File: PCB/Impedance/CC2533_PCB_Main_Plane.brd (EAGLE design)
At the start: 69.5 x 40.3 mm, 34 parts

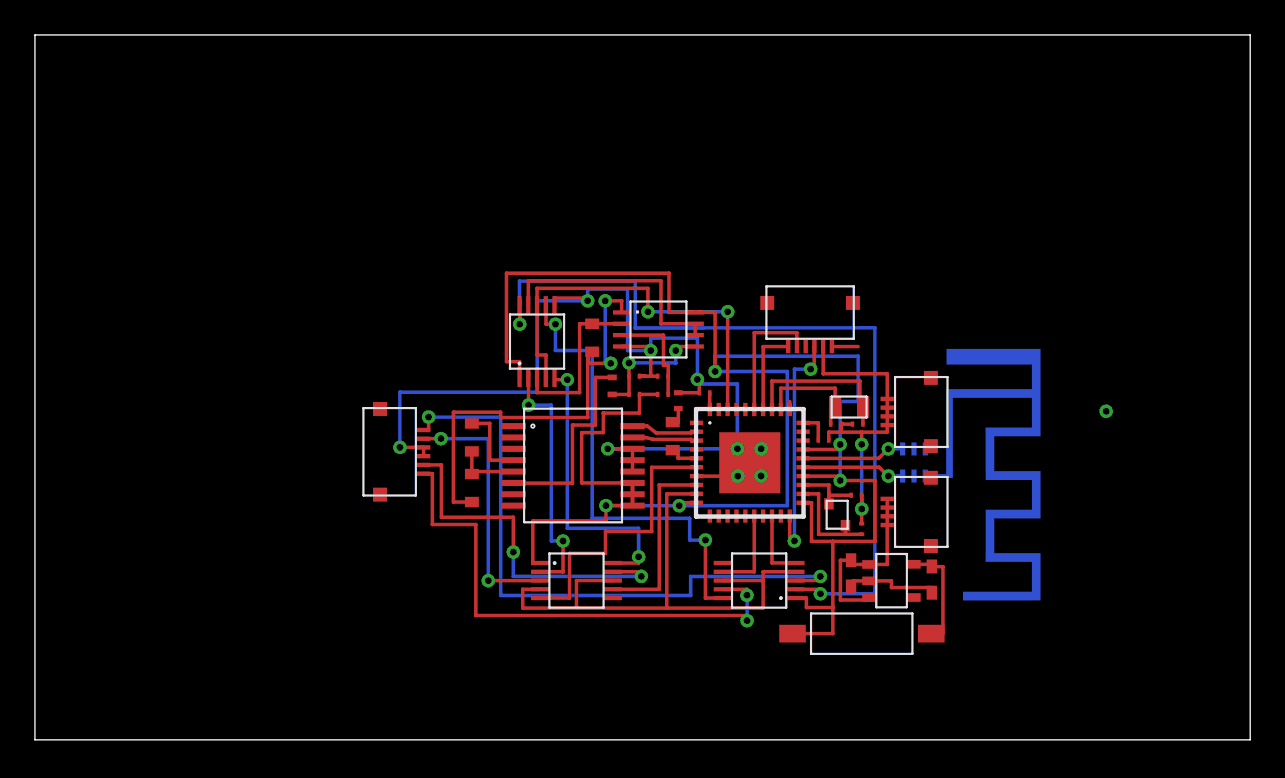
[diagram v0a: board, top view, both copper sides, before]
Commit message: New updates
Added new layout of CC2533 voltage stim and AD5933 impeance analysis
with ground planes (completed), and that of AD5933 impedance analysis
only.
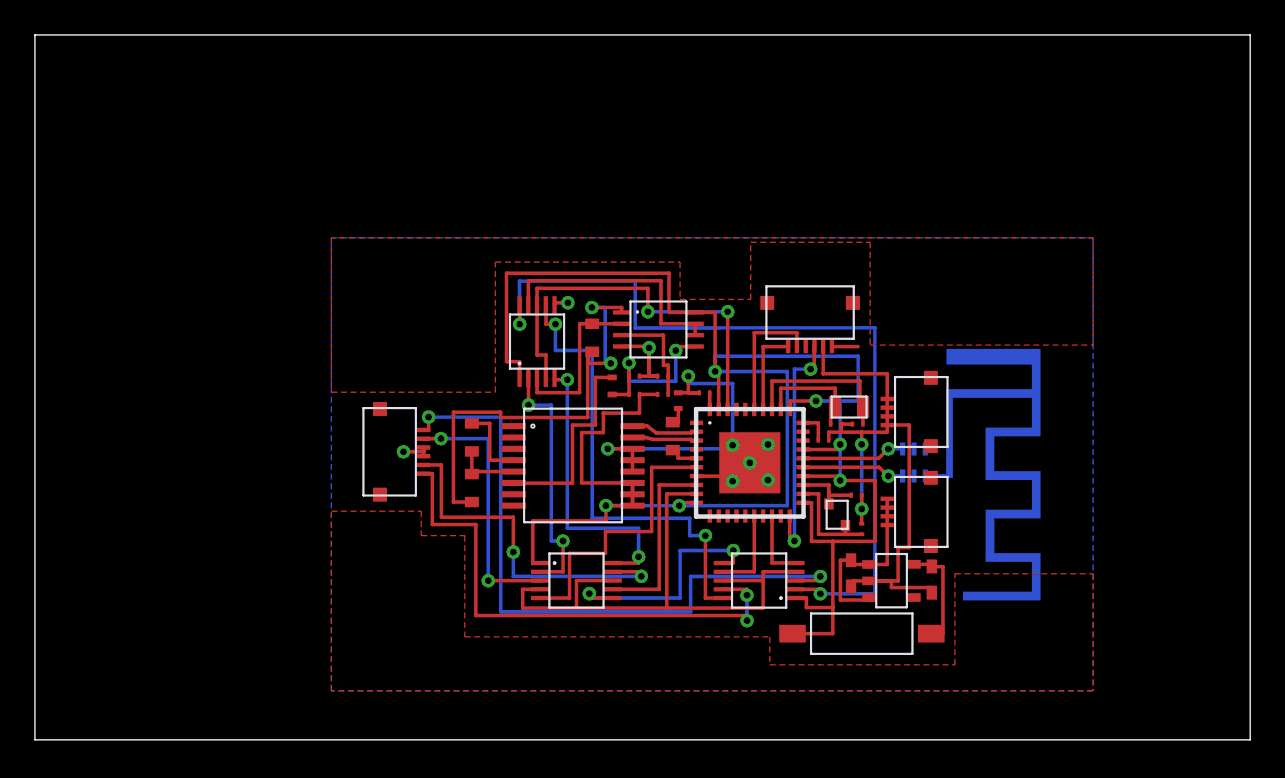
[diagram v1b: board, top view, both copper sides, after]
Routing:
- net VDD: track 119.2 -> 124.3 mm, vias 5 -> 6
- net GND: track 94.2 -> 97.2 mm, vias 12 -> 14
- net N$28: track 7.49 -> 9.59 mm
- net N$9: track 36.4 -> 38.2 mm
- net N$25: track 25.9 -> 26.7 mm
- added copper zone on layer 1, net GND
- added copper zone on layer 16, net GND

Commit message: Complete layouts for CC2533 circuits with AD5933
CC2533_PCB_Main_Plane - Voltage stim + Impedance Analysis.
CC2533_PCB_Biphasic - Current stim + Impedance Analysis.
CC2533_PCB_AD5933 - Impedance Analysis only.
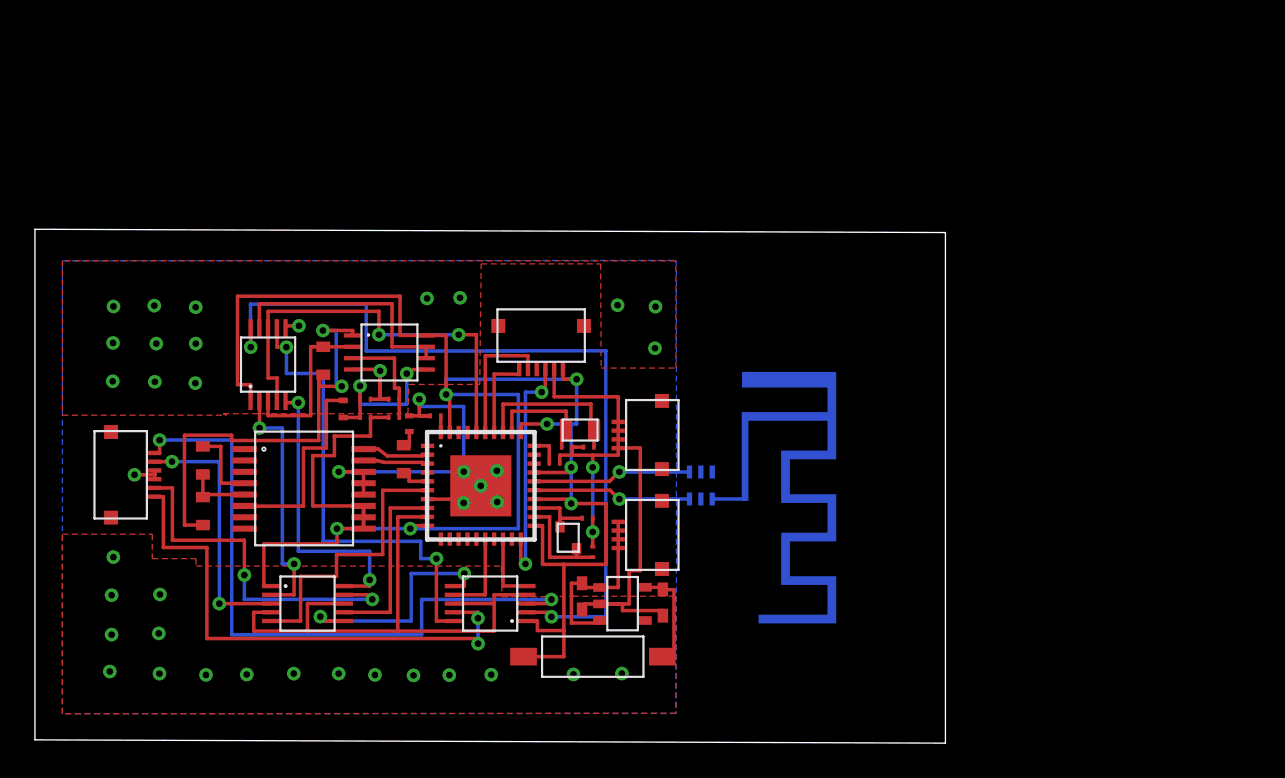
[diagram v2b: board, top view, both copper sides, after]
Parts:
- moved U$29 15.4 mm to (21.1, 16.1)
- moved U$12 15.4 mm to (31.3, 8.21)
- moved U$16 15.4 mm to (15.3, 14.4)
- moved U$17 15.4 mm to (28.9, 21.2)
- moved U$21 15.4 mm to (9.61, 16.0)
- moved U$22 15.4 mm to (9.61, 13.1)
- moved U$26 15.4 mm to (17.6, 18.9)
- moved U$27 15.4 mm to (18.9, 18.4)
- moved U$28 15.4 mm to (18.9, 19.5)
- moved U$30 15.4 mm to (6.84, 15.1)
- moved U$31 15.4 mm to (21.4, 18.1)
- moved U$4 15.4 mm to (31.9, 10.7)
- moved U$40 15.4 mm to (31.7, 16.7)
- moved U$5 15.4 mm to (31.6, 12.7)
- moved U$15 15.4 mm to (15.6, 7.80)
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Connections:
- net IN2: now also U$1.P2_0; no longer U$1.P1_6
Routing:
- net GND: track 97.2 -> 93.8 mm, vias 14 -> 45
- net N$1: track 5.93 -> 9.11 mm
- net N$2: track 5.93 -> 9.10 mm
- net VDD: track 124.3 -> 122.8 mm, vias 6 -> 7
- net IN2: track 23.5 -> 24.5 mm
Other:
- board size 69.5 x 40.3 mm -> 52.1 x 29.4 mm
